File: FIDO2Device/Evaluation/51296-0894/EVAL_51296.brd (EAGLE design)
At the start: 25 x 30 mm, 14 parts, among them CN1 51296-0894, CN2 IF_6PIN, CN3 IF_4PIN, Q1 BSS84AKQBZ, U1 RV-3028-C7

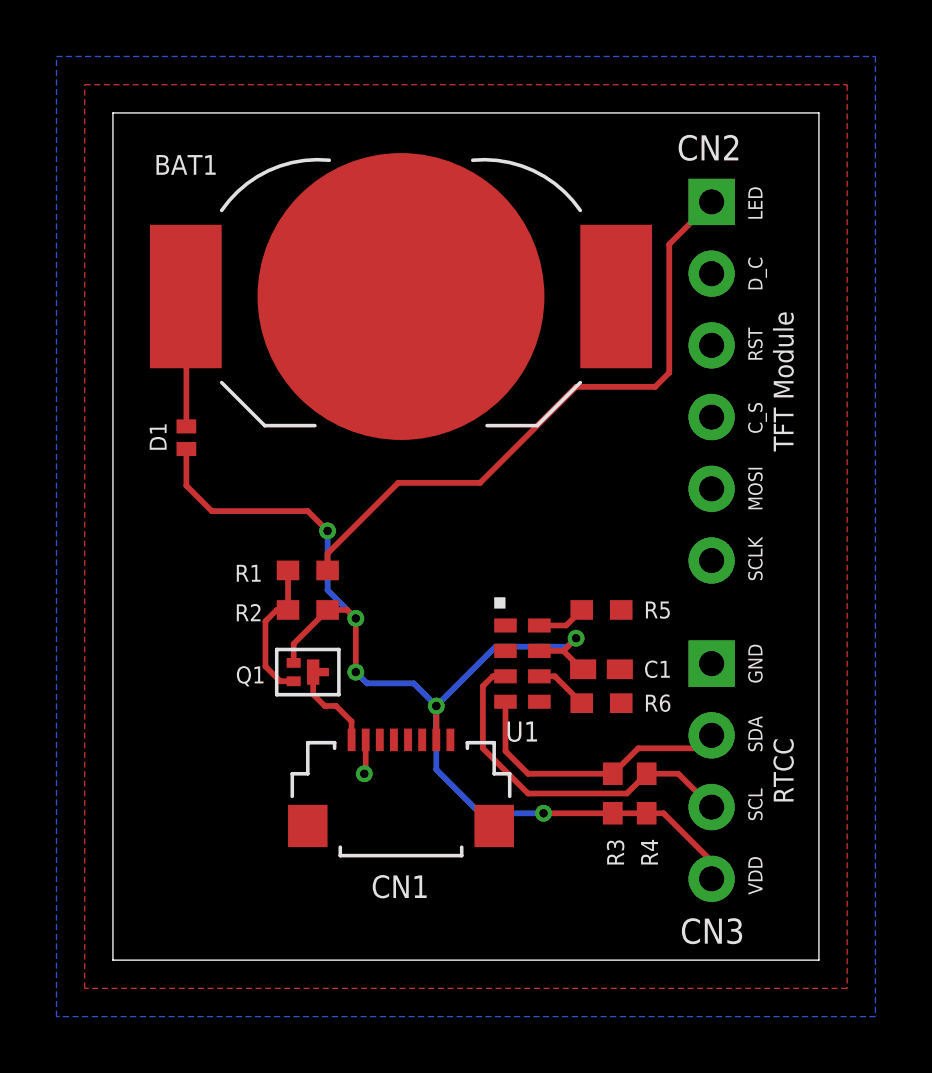
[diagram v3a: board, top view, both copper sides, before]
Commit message: 配線レイアウトを作成
・TFTモジュール接続用GPIOの配線
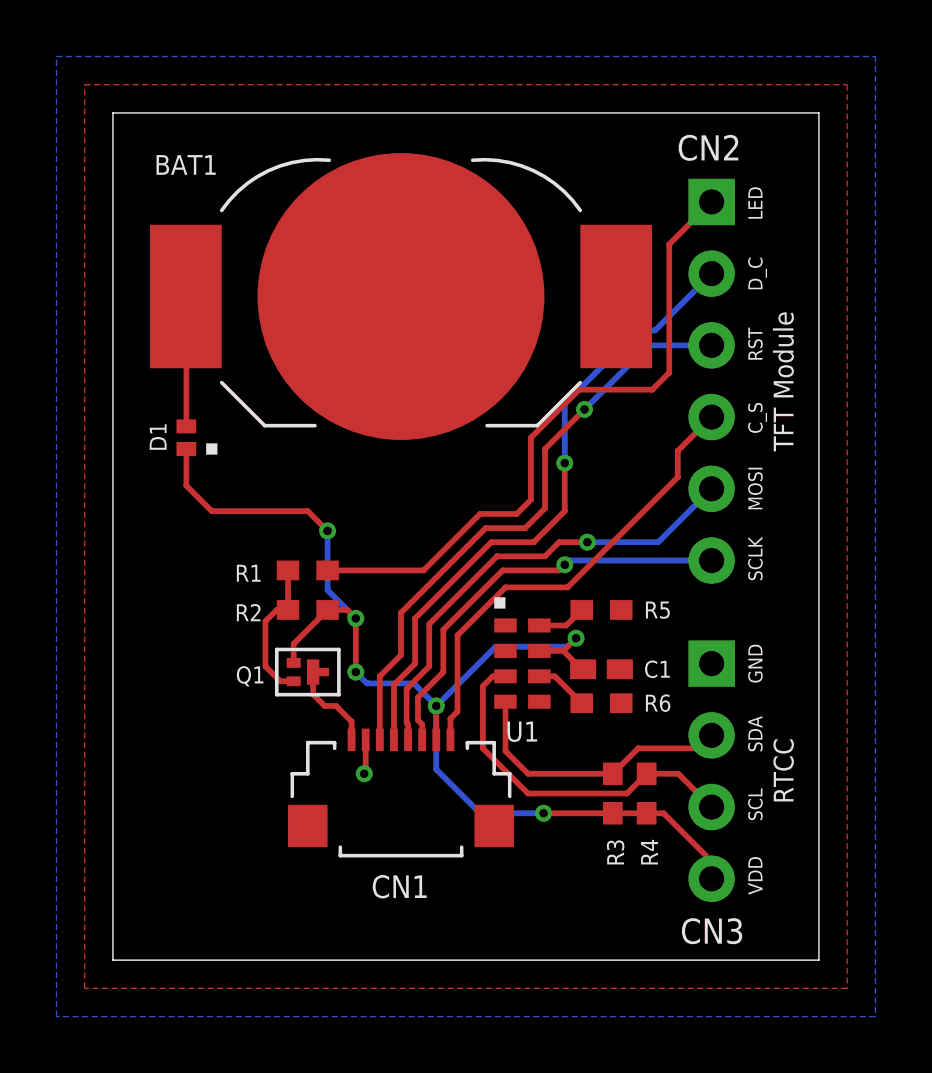
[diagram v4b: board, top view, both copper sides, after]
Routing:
- net D_C: track 0.00 -> 22.4 mm, vias 0 -> 1
- net RESET: track 0.00 -> 21.0 mm, vias 0 -> 1
- net CS: track 0.00 -> 16.6 mm
- net MOSI: track 0.00 -> 16.4 mm, vias 0 -> 1
- net CLK: track 0.00 -> 14.8 mm, vias 0 -> 1
- net LED_CTRL: track 22.0 -> 23.0 mm
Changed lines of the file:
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@@
 <text x="23.4" y="20.5" size="0.7" layer="21" rot="R90" align="top-center">TFT Module</text>
 <text x="23.4" y="6.7" size="0.7" layer="21" rot="R90" align="top-center">RTCC</text>
+<rectangle x1="3.3" y1="17.9" x2="3.7" y2="18.3" layer="21"/>
 </plain>
 <attributes>
@@
 <contactref element="R1" pad="1"/>
 <contactref element="CN2" pad="1"/>
-<wire x1="7.6" y1="13.8" x2="7.6" y2="14.4" width="0.2032" layer="1"/>
-<wire x1="7.6" y1="14.4" x2="10.1" y2="16.9" width="0.2032" layer="1"/>
-<wire x1="10.1" y1="16.9" x2="13" y2="16.9" width="0.2032" layer="1"/>
 <wire x1="21.2" y1="26.85" x2="19.7" y2="25.35" width="0.2032" layer="1"/>
 <wire x1="19.7" y1="25.35" x2="19.7" y2="20.8" width="0.2032" layer="1"/>
-<wire x1="13" y1="16.9" x2="16.4" y2="20.3" width="0.2032" layer="1"/>
-<wire x1="16.4" y1="20.3" x2="19.2" y2="20.3" width="0.2032" layer="1"/>
-<wire x1="19.2" y1="20.3" x2="19.7" y2="20.8" width="0.2032" layer="1"/>
+<wire x1="19.1" y1="20.2" x2="19.7" y2="20.8" width="0.2032" layer="1"/>
+<wire x1="19.1" y1="20.2" x2="16.5" y2="20.2" width="0.2032" layer="1"/>
+<wire x1="16.5" y1="20.2" x2="14.8" y2="18.5" width="0.2032" layer="1"/>
+<wire x1="14.8" y1="18.5" x2="14.8" y2="16.3" width="0.2032" layer="1"/>
+<wire x1="14.8" y1="16.3" x2="14.3" y2="15.8" width="0.2032" layer="1"/>
+<wire x1="14.3" y1="15.8" x2="13" y2="15.8" width="0.2032" layer="1"/>
+<wire x1="13" y1="15.8" x2="11" y2="13.8" width="0.2032" layer="1"/>
+<wire x1="11" y1="13.8" x2="7.6" y2="13.8" width="0.2032" layer="1"/>
 </signal>
 <signal name="CS">
 <contactref element="CN1" pad="8"/>
 <contactref element="CN2" pad="4"/>
-<wire x1="11.95" y1="7.8" x2="21.2" y2="19.23" width="0" layer="19" extent="1-1"/>
+<wire x1="11.95" y1="7.8" x2="11.95" y2="8.55" width="0.2032" layer="1"/>
+<wire x1="11.95" y1="8.55" x2="12.2" y2="8.8" width="0.2032" layer="1"/>
+<wire x1="12.2" y1="8.8" x2="12.2" y2="11.5" width="0.2032" layer="1"/>
+<wire x1="12.2" y1="11.5" x2="13.9" y2="13.2" width="0.2032" layer="1"/>
+<wire x1="13.9" y1="13.2" x2="16.1" y2="13.2" width="0.2032" layer="1"/>
+<wire x1="16.1" y1="13.2" x2="20" y2="17.1" width="0.2032" layer="1"/>
+<wire x1="20" y1="17.1" x2="20" y2="18.03" width="0.2032" layer="1"/>
+<wire x1="21.2" y1="19.23" x2="20" y2="18.03" width="0.2032" layer="1"/>
 </signal>
 <signal name="CLK">
 <contactref element="CN1" pad="6"/>
 <contactref element="CN2" pad="6"/>
-<wire x1="10.95" y1="7.8" x2="21.2" y2="14.15" width="0" layer="19" extent="1-1"/>
+<wire x1="21.2" y1="14.15" x2="16.15" y2="14.15" width="0.2032" layer="16"/>
+<wire x1="16.15" y1="14.15" x2="16" y2="14" width="0.2032" layer="16"/>
+<via x="16" y="14" extent="1-16" drill="0.3"/>
+<wire x1="16" y1="14" x2="15.8" y2="13.8" width="0.2032" layer="1"/>
+<wire x1="15.8" y1="13.8" x2="13.8" y2="13.8" width="0.2032" layer="1"/>
+<wire x1="13.8" y1="13.8" x2="11.7" y2="11.7" width="0.2032" layer="1"/>
+<wire x1="11.7" y1="11.7" x2="11.7" y2="10.2" width="0.2032" layer="1"/>
+<wire x1="11.7" y1="10.2" x2="10.8" y2="9.3" width="0.2032" layer="1"/>
+<wire x1="10.95" y1="7.8" x2="10.95" y2="8.35" width="0.2032" layer="1"/>
+<wire x1="10.95" y1="8.35" x2="10.8" y2="8.5" width="0.2032" layer="1"/>
+<wire x1="10.8" y1="8.5" x2="10.8" y2="9.3" width="0.2032" layer="1"/>
 </signal>
 <signal name="MOSI">
 <contactref element="CN1" pad="5"/>
 <contactref element="CN2" pad="5"/>
-<wire x1="10.45" y1="7.8" x2="21.2" y2="16.69" width="0" layer="19" extent="1-1"/>
+<via x="16.8" y="14.8" extent="1-16" drill="0.3"/>
+<wire x1="10.45" y1="7.8" x2="10.45" y2="8.35" width="0.2032" layer="1"/>
+<wire x1="10.45" y1="8.35" x2="10.4" y2="8.4" width="0.2032" layer="1"/>
+<wire x1="10.4" y1="8.4" x2="10.4" y2="9.6" width="0.2032" layer="1"/>
+<wire x1="10.4" y1="9.6" x2="11.2" y2="10.4" width="0.2032" layer="1"/>
+<wire x1="11.2" y1="10.4" x2="11.2" y2="11.9" width="0.2032" layer="1"/>
+<wire x1="11.2" y1="11.9" x2="13.6" y2="14.3" width="0.2032" layer="1"/>
+<wire x1="16.8" y1="14.8" x2="19.31" y2="14.8" width="0.2032" layer="16"/>
+<wire x1="19.31" y1="14.8" x2="21.2" y2="16.69" width="0.2032" layer="16"/>
+<wire x1="13.6" y1="14.3" x2="15.3" y2="14.3" width="0.2032" layer="1"/>
+<wire x1="15.3" y1="14.3" x2="15.8" y2="14.8" width="0.2032" layer="1"/>
+<wire x1="15.8" y1="14.8" x2="16.8" y2="14.8" width="0.2032" layer="1"/>
 </signal>
 <signal name="D_C">
 <contactref element="CN1" pad="4"/>
 <contactref element="CN2" pad="2"/>
-<wire x1="9.95" y1="7.8" x2="21.2" y2="24.31" width="0" layer="19" extent="1-1"/>
+<wire x1="16" y1="19.7" x2="16" y2="17.6" width="0.2032" layer="16"/>
+<via x="16" y="17.6" extent="1-16" drill="0.3"/>
+<wire x1="16" y1="19.7" x2="18.6" y2="22.3" width="0.2032" layer="16"/>
+<wire x1="18.6" y1="22.3" x2="19.2" y2="22.3" width="0.2032" layer="16"/>
+<wire x1="19.2" y1="22.3" x2="21.2" y2="24.3" width="0.2032" layer="16"/>
+<wire x1="21.2" y1="24.3" x2="21.2" y2="24.31" width="0.2032" layer="16"/>
+<wire x1="9.95" y1="7.8" x2="9.95" y2="9.75" width="0.2032" layer="1"/>
+<wire x1="9.95" y1="9.75" x2="10.7" y2="10.5" width="0.2032" layer="1"/>
+<wire x1="10.7" y1="10.5" x2="10.7" y2="12.1" width="0.2032" layer="1"/>
+<wire x1="10.7" y1="12.1" x2="13.4" y2="14.8" width="0.2032" layer="1"/>
+<wire x1="13.4" y1="14.8" x2="14.9" y2="14.8" width="0.2032" layer="1"/>
+<wire x1="14.9" y1="14.8" x2="16" y2="15.9" width="0.2032" layer="1"/>
+<wire x1="16" y1="17.6" x2="16" y2="15.9" width="0.2032" layer="1"/>
 </signal>
 <signal name="RESET">
 <contactref element="CN1" pad="3"/>
 <contactref element="CN2" pad="3"/>
-<wire x1="9.45" y1="7.8" x2="21.2" y2="21.77" width="0" layer="19" extent="1-1"/>
+<wire x1="21.2" y1="21.77" x2="18.97" y2="21.77" width="0.2032" layer="16"/>
+<wire x1="18.97" y1="21.77" x2="16.7" y2="19.5" width="0.2032" layer="16"/>
+<via x="16.7" y="19.5" extent="1-16" drill="0.3"/>
+<wire x1="16.7" y1="19.5" x2="15.3" y2="18.1" width="0.2032" layer="1"/>
+<wire x1="13.2" y1="15.3" x2="10.2" y2="12.3" width="0.2032" layer="1"/>
+<wire x1="10.2" y1="12.3" x2="10.2" y2="10.8" width="0.2032" layer="1"/>
+<wire x1="10.2" y1="10.8" x2="9.45" y2="10.05" width="0.2032" layer="1"/>
+<wire x1="9.45" y1="10.05" x2="9.45" y2="7.8" width="0.2032" layer="1"/>
+<wire x1="13.2" y1="15.3" x2="14.6" y2="15.3" width="0.2032" layer="1"/>
+<wire x1="14.6" y1="15.3" x2="15.3" y2="16" width="0.2032" layer="1"/>
+<wire x1="15.3" y1="16" x2="15.3" y2="18.1" width="0.2032" layer="1"/>
 </signal>
 <signal name="TWI_SDA">

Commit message: 配線レイアウトを作成
・回路に追加されたSBDを配置／配線
・TFTモジュール接続用GPIOの配線を見直し
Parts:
- added D2: PMEG2005BELD,315, Parts:DFN1006D-2
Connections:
- new net VDD: C1.1, CN1.7, D1.1, D2.1, Q1.2, R2.2, R3.2, R4.2, U1.7
- net VDD_NRF: now also D2.2; no longer C1.1, CN1.7, D1.1, Q1.2, R2.2, R3.2, R4.2, U1.7
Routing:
- net VDD: track 0.00 -> 41.8 mm, vias 0 -> 6
- net VDD_NRF: track 43.0 -> 4.41 mm, vias 6 -> 0
- net D_C: track 22.4 -> 23.3 mm
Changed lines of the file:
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@@
 <layer number="49" name="Reference" color="7" fill="1" visible="no" active="yes"/>
 <layer number="50" name="dxf" color="7" fill="1" visible="no" active="no"/>
-<layer number="51" name="tDocu" color="7" fill="1" visible="no" active="yes"/>
+<layer number="51" name="tDocu" color="7" fill="1" visible="yes" active="yes"/>
 <layer number="52" name="bDocu" color="7" fill="1" visible="yes" active="yes"/>
 <layer number="53" name="tGND_GNDA" color="7" fill="9" visible="no" active="no"/>
@@
 <wire x1="25" y1="30" x2="0" y2="30" width="0" layer="20"/>
 <wire x1="0" y1="30" x2="0" y2="0" width="0" layer="20"/>
-<rectangle x1="3" y1="1" x2="17" y2="29" layer="51"/>
-<rectangle x1="19" y1="1" x2="24" y2="29" layer="51"/>
 <text x="22.5" y="3" size="0.5" layer="21" rot="R90" align="top-center">VDD</text>
 <text x="22.5" y="5.5" size="0.5" layer="21" rot="R90" align="top-center">SCL</text>
@@
 <attribute name="VALUE" x="3.3" y="17.8" size="0.6" layer="27" rot="R90" align="top-left"/>
 </element>
+<element name="D2" library="Parts" package="DFN1006D-2" value="PMEG2005BELD,315" x="16.4" y="2.9"/>
 </elements>
 <signals>
@@
 <wire x1="5.8" y1="12.4" x2="5.4" y2="12" width="0.2032" layer="1"/>
 </signal>
-<signal name="VDD_NRF">
+<signal name="VDD">
 <contactref element="R2" pad="2"/>
 <contactref element="Q1" pad="2"/>
 <contactref element="CN1" pad="7"/>
-<contactref element="CN3" pad="4"/>
 <contactref element="R3" pad="2"/>
 <contactref element="C1" pad="1"/>
@@
 <via x="8.6" y="12.1" extent="1-16" drill="0.3"/>
 <via x="11.45" y="9" extent="1-16" drill="0.3"/>
-<via x="7.6" y="15.2" extent="1-16" drill="0.3"/>
+<via x="6.6" y="16" extent="1-16" drill="0.3"/>
 <via x="15.25" y="5.2" extent="1-16" drill="0.3"/>
-<wire x1="3.5" y1="15.9" x2="6.9" y2="15.9" width="0.2032" layer="1"/>
-<wire x1="3.5" y1="15.9" x2="2.6" y2="16.8" width="0.2032" layer="1"/>
-<wire x1="2.6" y1="16.8" x2="2.6" y2="18.1" width="0.2032" layer="1"/>
-<wire x1="7.6" y1="15.2" x2="6.9" y2="15.9" width="0.2032" layer="1"/>
-<wire x1="8.6" y1="12.1" x2="7.6" y2="13.1" width="0.2032" layer="16"/>
-<wire x1="7.6" y1="13.1" x2="7.6" y2="15.2" width="0.2032" layer="16"/>
+<wire x1="8.6" y1="12.1" x2="6.9" y2="13.8" width="0.2032" layer="16"/>
 <wire x1="8.6" y1="12.1" x2="8.4" y2="12.2" width="0.2032" layer="1"/>
 <wire x1="7.6" y1="12.4" x2="8.3" y2="12.4" width="0.2032" layer="1"/>
 <wire x1="8.3" y1="12.4" x2="8.6" y2="12.1" width="0.2032" layer="1"/>
-<via x="8.6" y="10.2" extent="1-16" drill="0.3"/>
-<wire x1="8.6" y1="10.2" x2="9" y2="9.8" width="0.2032" layer="16"/>
+<via x="8.8" y="10" extent="1-16" drill="0.3"/>
 <wire x1="9" y1="9.8" x2="10.65" y2="9.8" width="0.2032" layer="16"/>
 <wire x1="11.45" y1="9" x2="10.65" y2="9.8" width="0.2032" layer="16"/>
@@
 <wire x1="13" y1="5.2" x2="11.45" y2="6.75" width="0.2032" layer="16"/>
 <wire x1="11.45" y1="9" x2="11.45" y2="6.75" width="0.2032" layer="16"/>
-<wire x1="21.2" y1="2.88" x2="21.2" y2="3.5" width="0.2032" layer="1"/>
-<wire x1="21.2" y1="3.5" x2="19.5" y2="5.2" width="0.2032" layer="1"/>
-<wire x1="18.9" y1="5.2" x2="19.5" y2="5.2" width="0.2032" layer="1"/>
 <wire x1="18.9" y1="5.2" x2="17.7" y2="5.2" width="0.2032" layer="1"/>
 <wire x1="15.25" y1="5.2" x2="17.7" y2="5.2" width="0.2032" layer="1"/>
@@
 <wire x1="16.65" y1="10.3" x2="16.6" y2="10.3" width="0.2032" layer="1"/>
 <wire x1="16.6" y1="10.3" x2="15.95" y2="10.95" width="0.2032" layer="1"/>
-<wire x1="8.6" y1="10.2" x2="8.6" y2="12.1" width="0.2032" layer="1"/>
 <wire x1="6.4" y1="10.525" x2="6.4" y2="11.2" width="0.2032" layer="1"/>
 <wire x1="6.4" y1="11.2" x2="7.6" y2="12.4" width="0.2032" layer="1"/>
+<wire x1="2.6" y1="18.1" x2="2.6" y2="16.9" width="0.2032" layer="1"/>
+<wire x1="2.6" y1="16.9" x2="3" y2="16.5" width="0.2032" layer="1"/>
+<wire x1="3" y1="16.5" x2="6.1" y2="16.5" width="0.2032" layer="1"/>
+<wire x1="6.9" y1="13.8" x2="6.9" y2="15.7" width="0.2032" layer="16"/>
+<wire x1="6.9" y1="15.7" x2="6.6" y2="16" width="0.2032" layer="16"/>
+<wire x1="6.1" y1="16.5" x2="6.6" y2="16" width="0.2032" layer="1"/>
+<wire x1="9" y1="9.8" x2="8.8" y2="10" width="0.2032" layer="16"/>
+<wire x1="8.6" y1="12.1" x2="8.6" y2="10.2" width="0.2032" layer="1"/>
+<wire x1="8.6" y1="10.2" x2="8.8" y2="10" width="0.2032" layer="1"/>
+<contactref element="D2" pad="1"/>
+<wire x1="16" y1="2.9" x2="16" y2="4.45" width="0.2032" layer="1"/>
+<wire x1="16" y1="4.45" x2="15.25" y2="5.2" width="0.2032" layer="1"/>
 </signal>
 <signal name="LED_CTRL">
 <contactref element="R1" pad="1"/>
 <contactref element="CN2" pad="1"/>
-<wire x1="21.2" y1="26.85" x2="19.7" y2="25.35" width="0.2032" layer="1"/>
-<wire x1="19.7" y1="25.35" x2="19.7" y2="20.8" width="0.2032" layer="1"/>
-<wire x1="19.1" y1="20.2" x2="19.7" y2="20.8" width="0.2032" layer="1"/>
-<wire x1="19.1" y1="20.2" x2="16.5" y2="20.2" width="0.2032" layer="1"/>
-<wire x1="16.5" y1="20.2" x2="14.8" y2="18.5" width="0.2032" layer="1"/>
-<wire x1="14.8" y1="18.5" x2="14.8" y2="16.3" width="0.2032" layer="1"/>
-<wire x1="14.8" y1="16.3" x2="14.3" y2="15.8" width="0.2032" layer="1"/>
+<wire x1="15" y1="16.5" x2="14.3" y2="15.8" width="0.2032" layer="1"/>
 <wire x1="14.3" y1="15.8" x2="13" y2="15.8" width="0.2032" layer="1"/>
 <wire x1="13" y1="15.8" x2="11" y2="13.8" width="0.2032" layer="1"/>
 <wire x1="11" y1="13.8" x2="7.6" y2="13.8" width="0.2032" layer="1"/>
+<wire x1="15" y1="16.5" x2="17.3" y2="16.5" width="0.2032" layer="1"/>
+<wire x1="17.3" y1="16.5" x2="17.9" y2="17.1" width="0.2032" layer="1"/>
+<wire x1="17.9" y1="17.1" x2="17.9" y2="17.6" width="0.2032" layer="1"/>
+<wire x1="17.9" y1="17.6" x2="19.1" y2="18.8" width="0.2032" layer="1"/>
+<wire x1="19.1" y1="18.8" x2="19.1" y2="19.7" width="0.2032" layer="1"/>
+<wire x1="19.1" y1="19.7" x2="19.9" y2="20.5" width="0.2032" layer="1"/>
+<wire x1="19.9" y1="20.5" x2="19.9" y2="25.5" width="0.2032" layer="1"/>
+<wire x1="19.9" y1="25.5" x2="21.2" y2="26.8" width="0.2032" layer="1"/>
+<wire x1="21.2" y1="26.8" x2="21.2" y2="26.85" width="0.2032" layer="1"/>
 </signal>
 <signal name="CS">
@@
 <contactref element="CN1" pad="4"/>
 <contactref element="CN2" pad="2"/>
-<wire x1="16" y1="19.7" x2="16" y2="17.6" width="0.2032" layer="16"/>
-<via x="16" y="17.6" extent="1-16" drill="0.3"/>
-<wire x1="16" y1="19.7" x2="18.6" y2="22.3" width="0.2032" layer="16"/>
-<wire x1="18.6" y1="22.3" x2="19.2" y2="22.3" width="0.2032" layer="16"/>
-<wire x1="19.2" y1="22.3" x2="21.2" y2="24.3" width="0.2032" layer="16"/>
-<wire x1="21.2" y1="24.3" x2="21.2" y2="24.31" width="0.2032" layer="16"/>
+<via x="19.1" y="17.2" extent="1-16" drill="0.3"/>
 <wire x1="9.95" y1="7.8" x2="9.95" y2="9.75" width="0.2032" layer="1"/>
 <wire x1="9.95" y1="9.75" x2="10.7" y2="10.5" width="0.2032" layer="1"/>
@@
 <wire x1="10.7" y1="12.1" x2="13.4" y2="14.8" width="0.2032" layer="1"/>
 <wire x1="13.4" y1="14.8" x2="14.9" y2="14.8" width="0.2032" layer="1"/>
-<wire x1="14.9" y1="14.8" x2="16" y2="15.9" width="0.2032" layer="1"/>
-<wire x1="16" y1="17.6" x2="16" y2="15.9" width="0.2032" layer="1"/>
+<wire x1="21.2" y1="24.31" x2="19.9" y2="23.01" width="0.2032" layer="16"/>
+<wire x1="19.9" y1="23.01" x2="19.9" y2="20.5" width="0.2032" layer="16"/>
+<wire x1="14.9" y1="14.8" x2="15.6" y2="15.5" width="0.2032" layer="1"/>
+<wire x1="15.6" y1="15.5" x2="17.7" y2="15.5" width="0.2032" layer="1"/>
+<wire x1="17.7" y1="15.5" x2="19.1" y2="16.9" width="0.2032" layer="1"/>
+<wire x1="19.9" y1="20.5" x2="19.1" y2="19.7" width="0.2032" layer="16"/>
+<wire x1="19.1" y1="16.9" x2="19.1" y2="17.2" width="0.2032" layer="1"/>
+<wire x1="19.1" y1="19.7" x2="19.1" y2="17.2" width="0.2032" layer="16"/>
 </signal>
 <signal name="RESET">
 <contactref element="CN1" pad="3"/>
 <contactref element="CN2" pad="3"/>
-<wire x1="21.2" y1="21.77" x2="18.97" y2="21.77" width="0.2032" layer="16"/>
-<wire x1="18.97" y1="21.77" x2="16.7" y2="19.5" width="0.2032" layer="16"/>
-<via x="16.7" y="19.5" extent="1-16" drill="0.3"/>
-<wire x1="16.7" y1="19.5" x2="15.3" y2="18.1" width="0.2032" layer="1"/>
+<via x="19.7" y="19.4" extent="1-16" drill="0.3"/>
 <wire x1="13.2" y1="15.3" x2="10.2" y2="12.3" width="0.2032" layer="1"/>
 <wire x1="10.2" y1="12.3" x2="10.2" y2="10.8" width="0.2032" layer="1"/>
@@
 <wire x1="13.2" y1="15.3" x2="14.6" y2="15.3" width="0.2032" layer="1"/>
 <wire x1="14.6" y1="15.3" x2="15.3" y2="16" width="0.2032" layer="1"/>
-<wire x1="15.3" y1="16" x2="15.3" y2="18.1" width="0.2032" layer="1"/>
+<wire x1="21.2" y1="21.77" x2="21.2" y2="20.9" width="0.2032" layer="16"/>
+<wire x1="21.2" y1="20.9" x2="19.7" y2="19.4" width="0.2032" layer="16"/>
+<wire x1="18.4" y1="16.9" x2="17.5" y2="16" width="0.2032" layer="1"/>
+<wire x1="17.5" y1="16" x2="15.3" y2="16" width="0.2032" layer="1"/>
+<wire x1="18.4" y1="17.4" x2="18.4" y2="16.9" width="0.2032" layer="1"/>
+<wire x1="18.4" y1="17.4" x2="19.7" y2="18.7" width="0.2032" layer="1"/>
+<wire x1="19.7" y1="18.7" x2="19.7" y2="19.4" width="0.2032" layer="1"/>
 </signal>
 <signal name="TWI_SDA">
@@
 <wire x1="2.6" y1="23.48" x2="2.6" y2="18.9" width="0.2032" layer="1"/>
 </signal>
+<signal name="VDD_NRF">
+<contactref element="D2" pad="2"/>
+<contactref element="CN3" pad="4"/>
+<wire x1="21.2" y1="2.88" x2="16.82" y2="2.88" width="0.2032" layer="1"/>
+<wire x1="16.82" y1="2.88" x2="16.8" y2="2.9" width="0.2032" layer="1"/>
+</signal>
 </signals>
